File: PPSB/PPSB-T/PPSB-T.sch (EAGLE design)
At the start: 7 parts

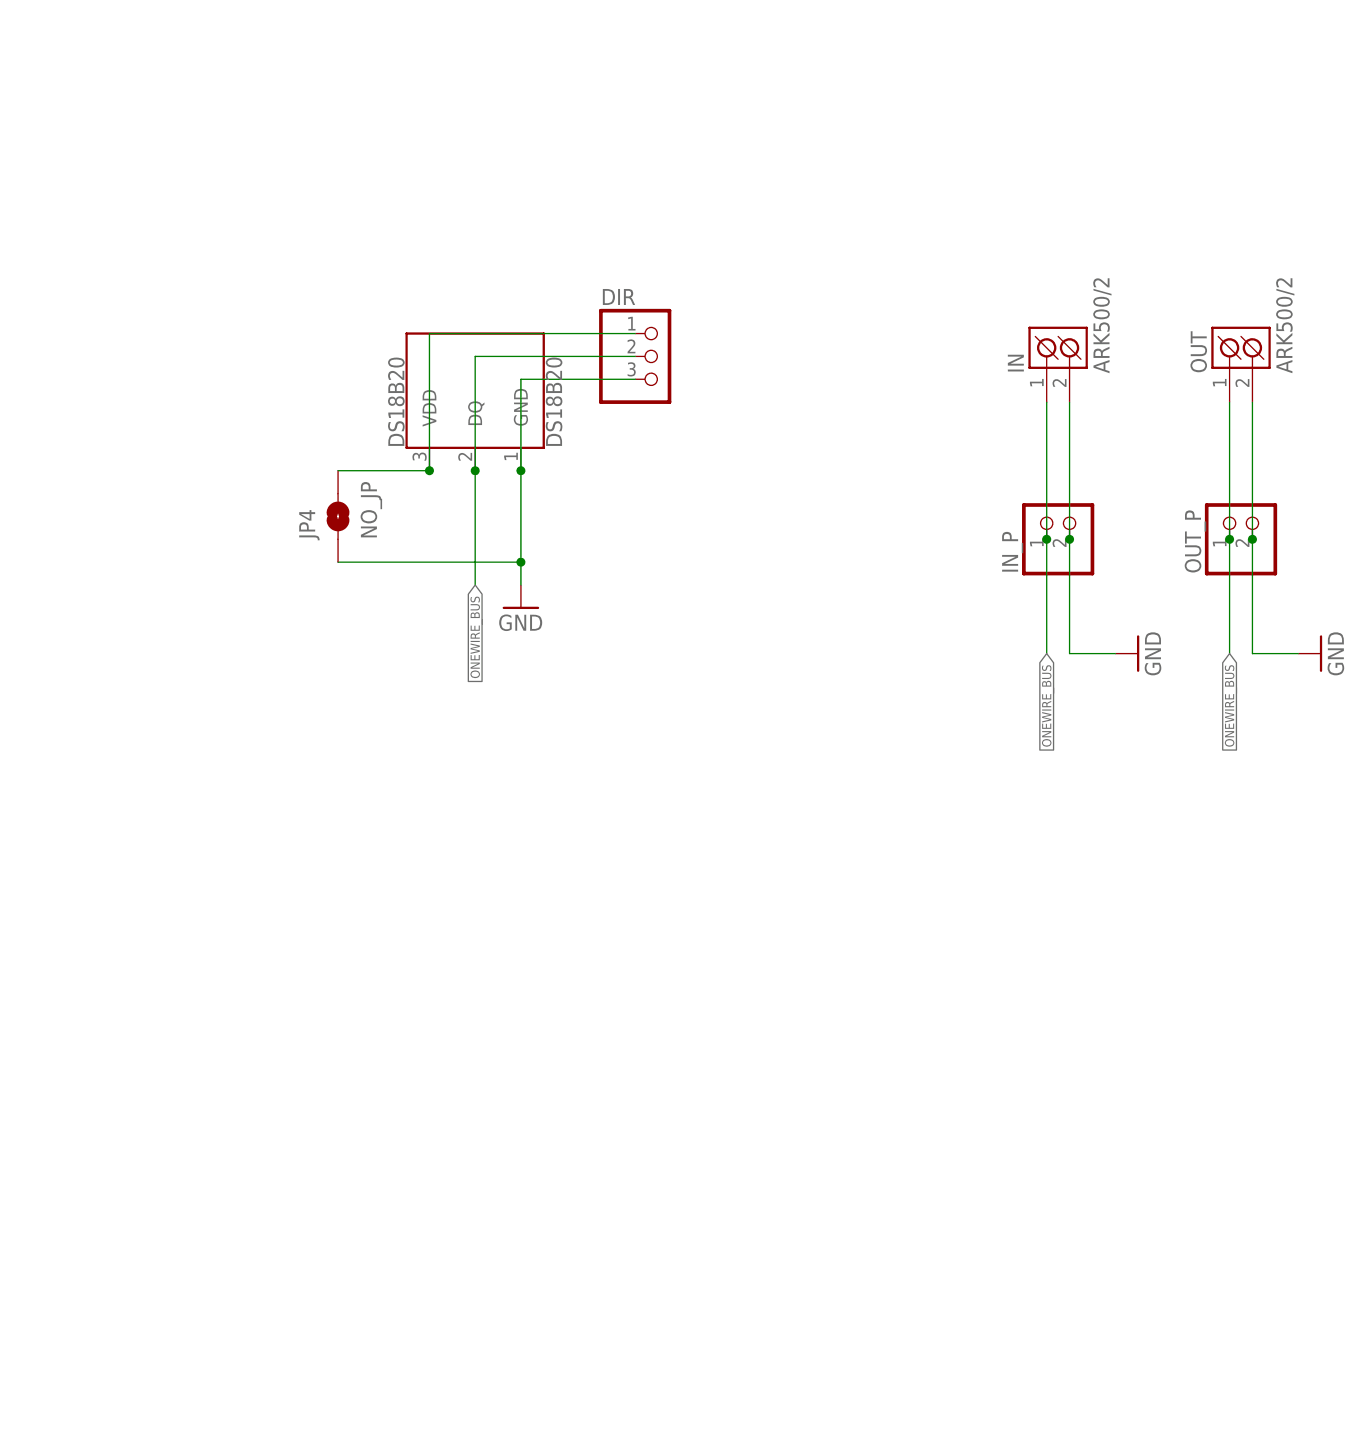
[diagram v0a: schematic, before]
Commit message: Updated PPSB-T  & PPSB-TH schematics. Add PanelBoard v1.
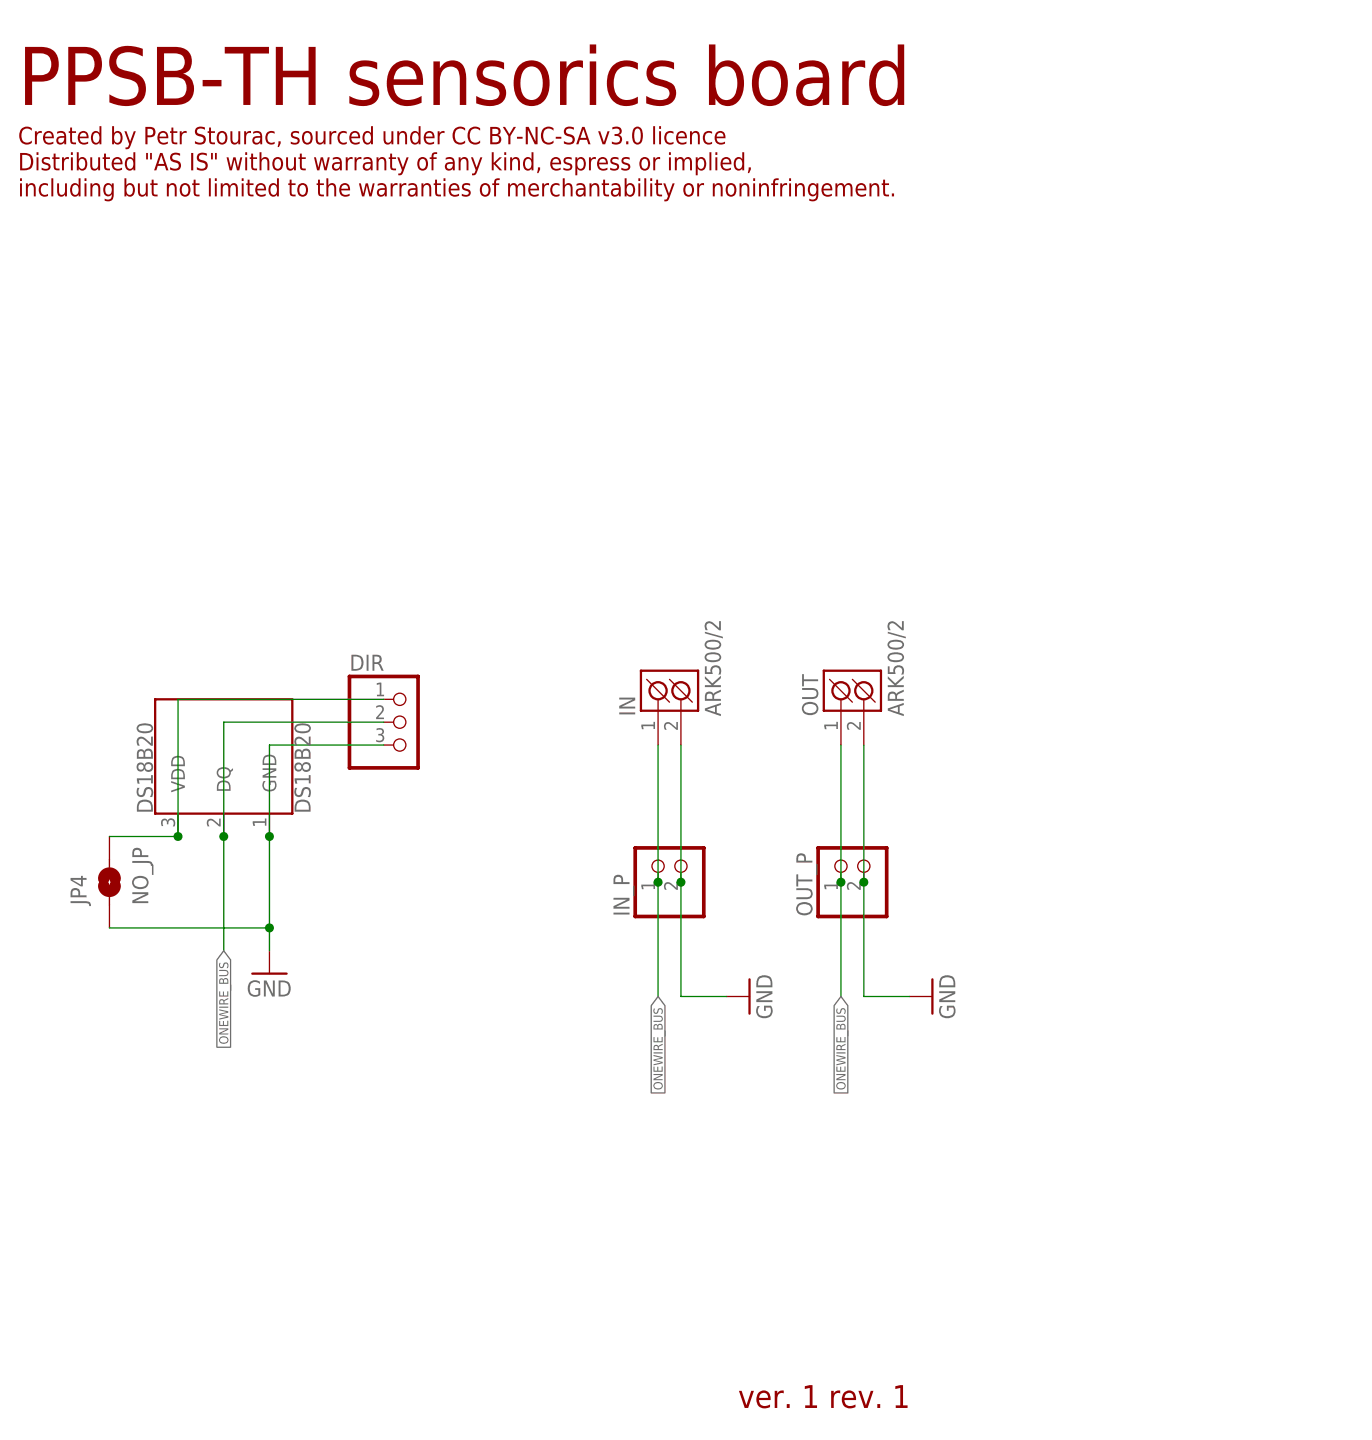
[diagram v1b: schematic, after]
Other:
- note added: "Created by Petr Stourac, sourced under CC BY-NC-SA v3.0 licence Distributed "AS IS" without warranty of any kind, espress or implied, including but not limited to the warranties of merchantability or noninfringement."
- note added: "PPSB-TH sensorics board"
- note added: "ver. 1 rev. 1"
- moved on the sheet: DIR, DS18B20, IN, IN_P, JP4, OUT, OUT_P
